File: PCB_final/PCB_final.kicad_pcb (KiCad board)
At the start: 4 copper layers, 90 x 95 mm, 120 parts, among them J1 02x30_Shift_Register_Connector, J2 02x30_ADC_Connector, J3 PicoPinSocketB, J4 PicoPinSocketA, U1 74HC595, U2 74HC595, U3 74HC595, U4 74HC595, U5 74HC595, U6 74HC595, U7 74HC595, U8 MAX11643EEG, U9 MAX11643EEG

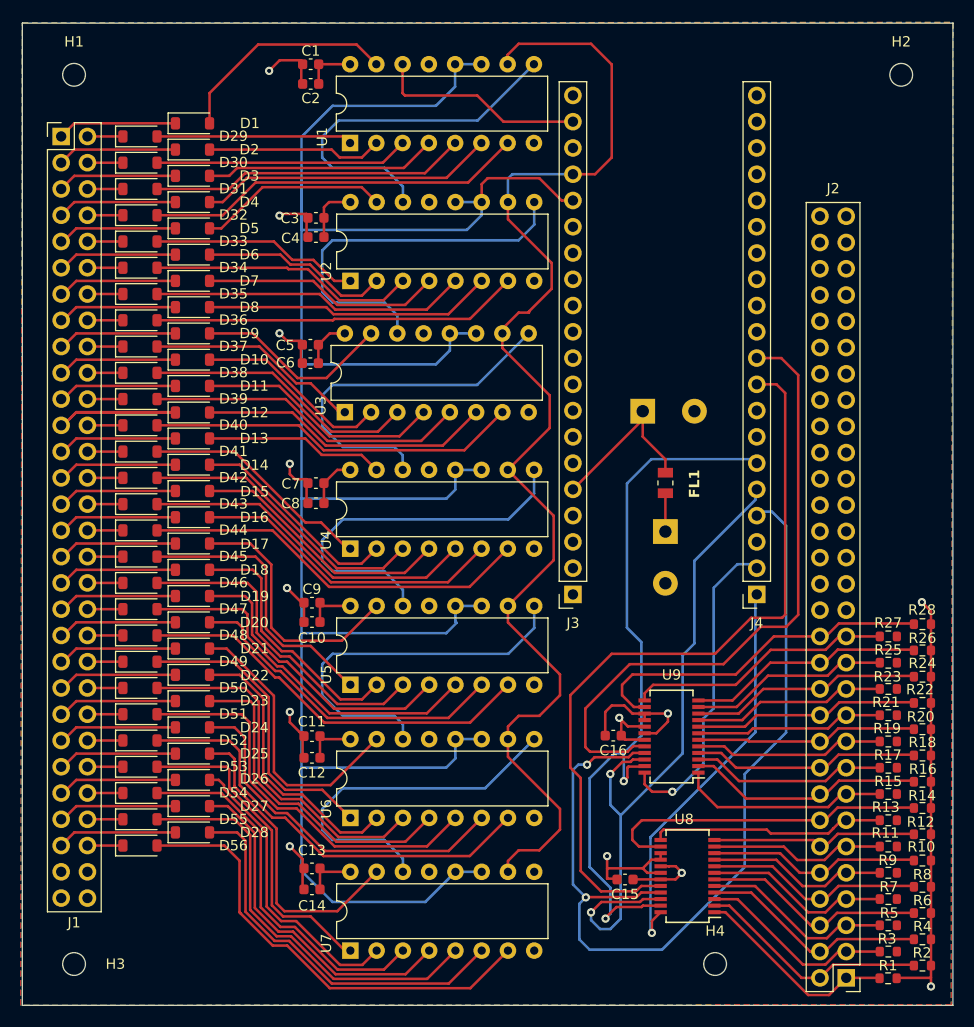
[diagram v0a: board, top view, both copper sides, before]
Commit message: Added 2 bypass capacitors for VREF pins on ADCs on schematic. Placed caps on PCB and rerouted traces to pass DRC. Increased trace thickness for 3v3 on ADCs to 0.35mm and 0.75mm going from PICO 3v3 to power supply filter to 3v3. Also re-arranged silkscreen to be visible when ribbon cable connectors are installed. Moved mounting holes to be accesible once ribbon cables are installed
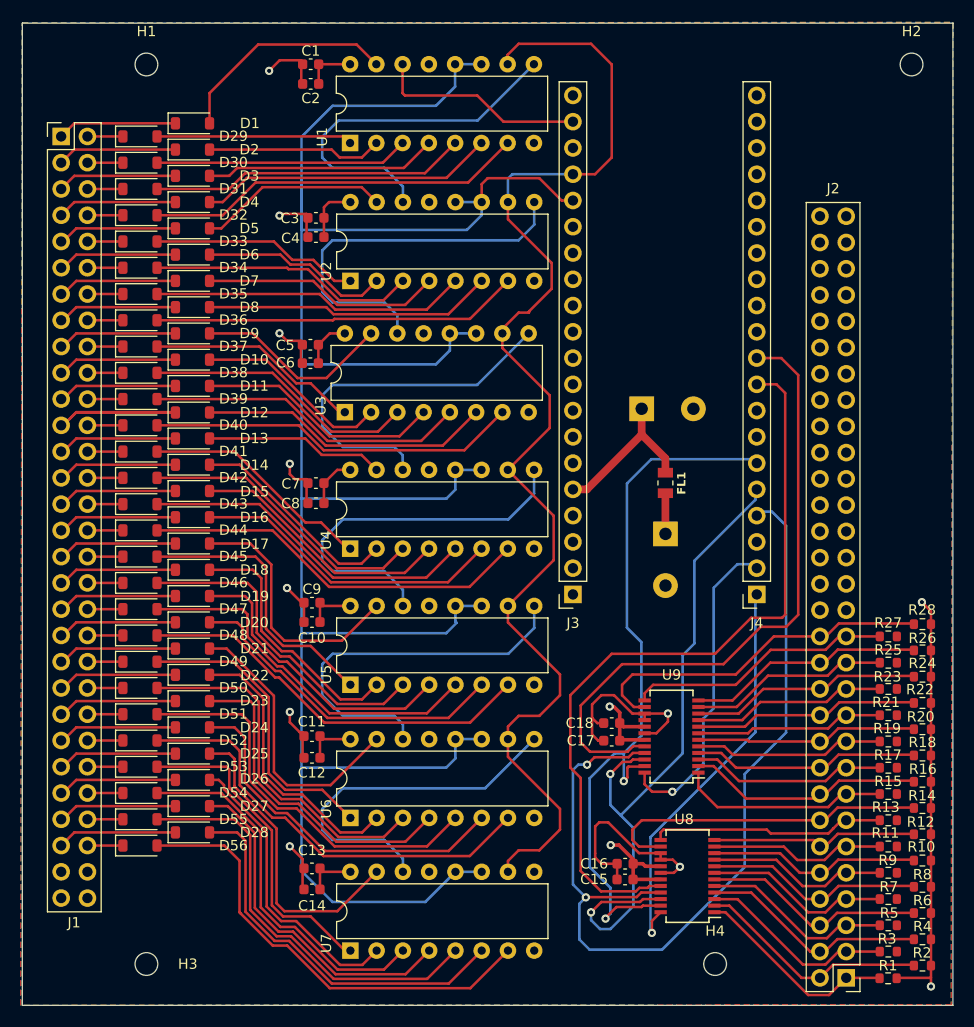
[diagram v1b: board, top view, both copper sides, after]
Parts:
- added C19: 4.7mF, Capacitor_THT:CP_Radial_D13.0mm_P5.00mm, B.Cu at (152.9, 97.3)
- added C20: 4.7mF, Capacitor_THT:CP_Radial_D13.0mm_P5.00mm, B.Cu at (155.2, 109.4)
- C17, C18: value 4.7mF -> .1uF; footprint Capacitor_THT:CP_Radial_D13.0mm_P5.00mm -> Capacitor_SMD:C_0603_1608Metric; moved to F.Cu
- moved C17 32.0 mm to (150.0, 129.4), turned to 180 degrees
- moved C18 19.2 mm to (150.0, 127.7), turned to 180 degrees
- moved C16 12.4 mm to (151.3, 141.3)
- moved H1 7.07 mm to (105.0, 64.0)
- moved H3 7.00 mm to (105.0, 151.0)
- moved H2 1.41 mm to (179.0, 64.0)
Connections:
- C17 pad 1: 3V3_Pico -> +3V3
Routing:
- net GND: track 97.4 -> 110.9 mm
- net +3V3: track 54.0 -> 58.6 mm
- net /Interface Board/SPI0_TX: track 67.3 -> 68.3 mm
- net /Interface Board/CS1: track 62.2 -> 63.0 mm

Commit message: Updated kicad PCB to use both SPI channels of the RPI Pico
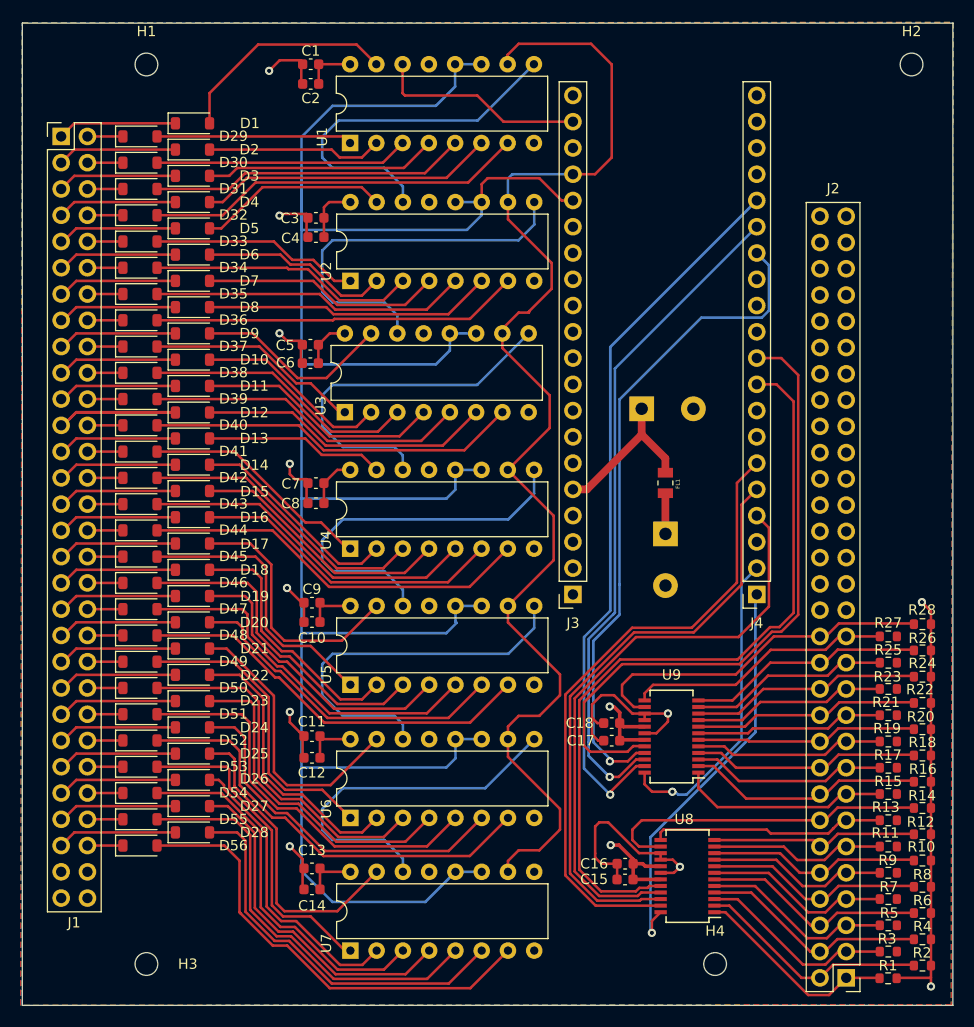
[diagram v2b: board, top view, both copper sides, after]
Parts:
- FL1: footprint BLM21BD272SN1L:BEADC2012X145N -> capstone_custom:BEADC2012X145N
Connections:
- J4 pad 14: unconnected-(J4-Pin_14-Pad14) -> /Interface Board/SPI1_SCK
- J4 pad 15: unconnected-(J4-Pin_15-Pad15) -> /Interface Board/SPI1_TX
- J4 pad 16: unconnected-(J4-Pin_16-Pad16) -> /Interface Board/SPI1_RX
- U9 pad 21: /Interface Board/SPI0_SCK -> /Interface Board/SPI1_SCK
- U9 pad 22: /Interface Board/SPI0_TX -> /Interface Board/SPI1_TX
- U9 pad 23: /Interface Board/SPI0_RX -> /Interface Board/SPI1_RX
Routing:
- net /Interface Board/SPI1_RX: track 0.00 -> 70.1 mm, vias 0 -> 1
- net /Interface Board/SPI1_TX: track 0.00 -> 64.9 mm, vias 0 -> 1
- net /Interface Board/SPI1_SCK: track 0.00 -> 64.5 mm, vias 0 -> 1
- net /Interface Board/SPI0_SCK: track 90.3 -> 57.9 mm, vias 2 -> 0
- net /Interface Board/SPI0_RX: track 71.8 -> 61.3 mm, vias 2 -> 0
- net /Interface Board/SPI0_TX: track 68.3 -> 57.9 mm, vias 2 -> 0
- net 3V3_Pico: track 16.8 -> 16.0 mm
